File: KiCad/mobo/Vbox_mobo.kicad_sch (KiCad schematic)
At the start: 38 parts, among them J1 Conn_01x02, J2 DuPont Connector, J2 JTAG_TC2030, J4 Conn_01x06, J5 Conn_01x06, J6 Conn_01x10, J7 Conn_01x10, SW1 Boot, U1 XC6206, U2 X05A26H12G, U3 RP2040, U4 W25Q128JVS, Y1 12MHz

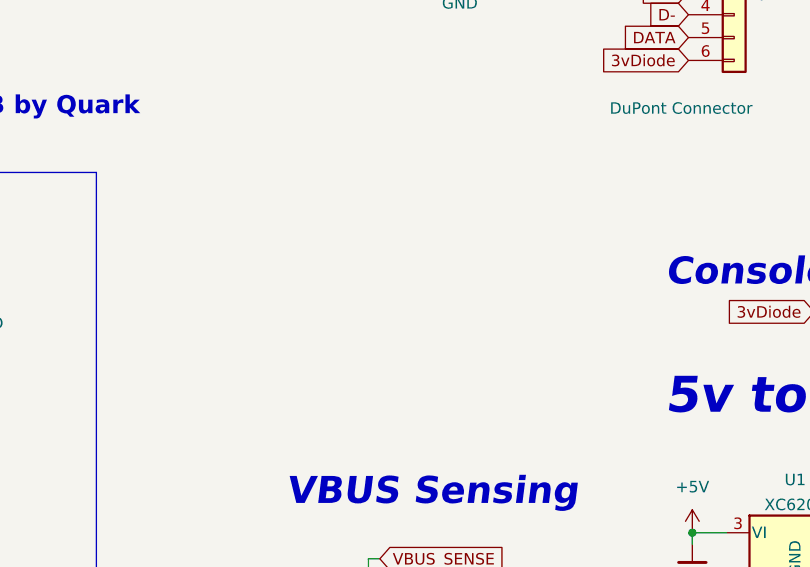
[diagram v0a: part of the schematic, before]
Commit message: replace vias with mounting holes
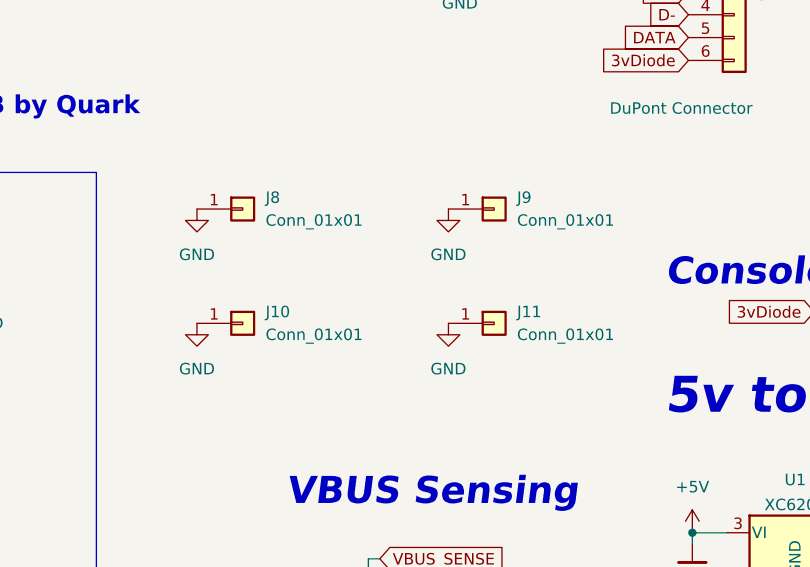
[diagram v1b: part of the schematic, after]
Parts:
- added J10, J11, J8, J9: Conn_01x01, MountingHole:MountingHole_3.2mm_M3_ISO14580_Pad_TopBottom, symbol Connector_Generic:Conn_01x01
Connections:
- net GND: now also J10.1 (Pin_1), J11.1 (Pin_1), J8.1 (Pin_1), J9.1 (Pin_1)
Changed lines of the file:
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@@
+    )
+  )
+  (symbol (lib_id "Connector_Generic:Conn_01x01") (at 190.5 125.73 0) (unit 1)
+    (in_bom yes) (on_board yes) (dnp no) (fields_autoplaced)
+    (property "Reference" "J10" (at 193.04 124.46 0)
+      (effects (font (size 1.27 1.27)) (justify left))
+    )
+    (property "Value" "Conn_01x01" (at 193.04 127 0)
+      (effects (font (size 1.27 1.27)) (justify left))
+    )
+    (property "Footprint" "MountingHole:MountingHole_3.2mm_M3_ISO14580_Pad_TopBottom" (at 190.5 125.73 0)
+      (effects (font (size 1.27 1.27)) hide)
+    )
+    (property "Datasheet" "~" (at 190.5 125.73 0)
+      (effects (font (size 1.27 1.27)) hide)
+    )
+    (pin "1")
+    (instances
+      (project "Vbox_mobo"
+        (path "/9f19960e-6523-4fd2-955a-272ad4648acf"
+          (reference "J10") (unit 1)
+        )
+      )
     )
   )
@@
     )
   )
+  (symbol (lib_name "GND_8") (lib_id "power:GND") (at 213.36 125.73 0) (unit 1)
+    (in_bom yes) (on_board yes) (dnp no) (fields_autoplaced)
+    (property "Reference" "#PWR032" (at 213.36 132.08 0)
+      (effects (font (size 1.27 1.27)) hide)
+    )
+    (property "Value" "GND" (at 213.36 130.81 0)
+      (effects (font (size 1.27 1.27)))
+    )
+    (property "Footprint" "" (at 213.36 125.73 0)
+      (effects (font (size 1.27 1.27)) hide)
+    )
+    (property "Datasheet" "" (at 213.36 125.73 0)
+      (effects (font (size 1.27 1.27)) hide)
+    )
+    (pin "1")
+    (instances
+      (project "Vbox_mobo"
+        (path "/9f19960e-6523-4fd2-955a-272ad4648acf"
+          (reference "#PWR032") (unit 1)
+        )
+      )
+    )
+  )
   (symbol (lib_id "Device:R_Small") (at 208.4578 157.48 90) (unit 1)
     (in_bom yes) (on_board yes) (dnp no)
@@
     )
   )
+  (symbol (lib_id "Connector_Generic:Conn_01x01") (at 190.5 113.03 0) (unit 1)
+    (in_bom yes) (on_board yes) (dnp no) (fields_autoplaced)
+    (property "Reference" "J8" (at 193.04 111.76 0)
+      (effects (font (size 1.27 1.27)) (justify left))
+    )
+    (property "Value" "Conn_01x01" (at 193.04 114.3 0)
+      (effects (font (size 1.27 1.27)) (justify left))
+    )
+    (property "Footprint" "MountingHole:MountingHole_3.2mm_M3_ISO14580_Pad_TopBottom" (at 190.5 113.03 0)
+      (effects (font (size 1.27 1.27)) hide)
+    )
+    (property "Datasheet" "~" (at 190.5 113.03 0)
+      (effects (font (size 1.27 1.27)) hide)
+    )
+    (pin "1")
+    (instances
+      (project "Vbox_mobo"
+        (path "/9f19960e-6523-4fd2-955a-272ad4648acf"
+          (reference "J8") (unit 1)
+        )
+      )
+    )
+  )
   (symbol (lib_id "power:+5V") (at 240.4618 148.9964 0) (unit 1)
     (in_bom yes) (on_board yes) (dnp no) (fields_autoplaced)
@@
     )
   )
+  (symbol (lib_name "GND_6") (lib_id "power:GND") (at 185.42 113.03 0) (unit 1)
+    (in_bom yes) (on_board yes) (dnp no) (fields_autoplaced)
+    (property "Reference" "#PWR013" (at 185.42 119.38 0)
+      (effects (font (size 1.27 1.27)) hide)
+    )
+    (property "Value" "GND" (at 185.42 118.11 0)
+      (effects (font (size 1.27 1.27)))
+    )
+    (property "Footprint" "" (at 185.42 113.03 0)
+      (effects (font (size 1.27 1.27)) hide)
+    )
+    (property "Datasheet" "" (at 185.42 113.03 0)
+      (effects (font (size 1.27 1.27)) hide)
+    )
+    (pin "1")
+    (instances
+      (project "Vbox_mobo"
+        (path "/9f19960e-6523-4fd2-955a-272ad4648acf"
+          (reference "#PWR013") (unit 1)
+        )
+      )
+    )
+  )
   (symbol (lib_id "Memory_Flash:W25Q128JVS") (at 144.145 137.16 0) (unit 1)
     (in_bom yes) (on_board yes) (dnp no)
@@
     )
   )
+  (symbol (lib_id "Connector_Generic:Conn_01x01") (at 218.44 125.73 0) (unit 1)
+    (in_bom yes) (on_board yes) (dnp no) (fields_autoplaced)
+    (property "Reference" "J11" (at 220.98 124.46 0)
+      (effects (font (size 1.27 1.27)) (justify left))
+    )
+    (property "Value" "Conn_01x01" (at 220.98 127 0)
+      (effects (font (size 1.27 1.27)) (justify left))
+    )
+    (property "Footprint" "MountingHole:MountingHole_3.2mm_M3_ISO14580_Pad_TopBottom" (at 218.44 125.73 0)
+      (effects (font (size 1.27 1.27)) hide)
+    )
+    (property "Datasheet" "~" (at 218.44 125.73 0)
+      (effects (font (size 1.27 1.27)) hide)
+    )
+    (pin "1")
+    (instances
+      (project "Vbox_mobo"
+        (path "/9f19960e-6523-4fd2-955a-272ad4648acf"
+          (reference "J11") (unit 1)
+        )
+      )
+    )
+  )
+  (symbol (lib_name "GND_9") (lib_id "power:GND") (at 185.42 125.73 0) (unit 1)
+    (in_bom yes) (on_board yes) (dnp no) (fields_autoplaced)
+    (property "Reference" "#PWR033" (at 185.42 132.08 0)
+      (effects (font (size 1.27 1.27)) hide)
+    )
+    (property "Value" "GND" (at 185.42 130.81 0)
+      (effects (font (size 1.27 1.27)))
+    )
+    (property "Footprint" "" (at 185.42 125.73 0)
+      (effects (font (size 1.27 1.27)) hide)
+    )
+    (property "Datasheet" "" (at 185.42 125.73 0)
+      (effects (font (size 1.27 1.27)) hide)
+    )
+    (pin "1")
+    (instances
+      (project "Vbox_mobo"
+        (path "/9f19960e-6523-4fd2-955a-272ad4648acf"
+          (reference "#PWR033") (unit 1)
+        )
+      )
+    )
+  )
+  (symbol (lib_id "Connector_Generic:Conn_01x01") (at 218.44 113.03 0) (unit 1)
+    (in_bom yes) (on_board yes) (dnp no) (fields_autoplaced)
+    (property "Reference" "J9" (at 220.98 111.76 0)
+      (effects (font (size 1.27 1.27)) (justify left))
+    )
+    (property "Value" "Conn_01x01" (at 220.98 114.3 0)
+      (effects (font (size 1.27 1.27)) (justify left))
+    )
+    (property "Footprint" "MountingHole:MountingHole_3.2mm_M3_ISO14580_Pad_TopBottom" (at 218.44 113.03 0)
+      (effects (font (size 1.27 1.27)) hide)
+    )
+    (property "Datasheet" "~" (at 218.44 113.03 0)
+      (effects (font (size 1.27 1.27)) hide)
+    )
+    (pin "1")
+    (instances
+      (project "Vbox_mobo"
+        (path "/9f19960e-6523-4fd2-955a-272ad4648acf"
+          (reference "J9") (unit 1)
+        )
+      )
+    )
+  )
   (symbol (lib_id "power:GND") (at 74.676 171.704 0) (unit 1)
     (in_bom yes) (on_board yes) (dnp no) (fields_autoplaced)
@@
         )
       )
+    )
+  )
+  (symbol (lib_name "GND_7") (lib_id "power:GND") (at 213.36 113.03 0) (unit 1)
+    (in_bom yes) (on_board yes) (dnp no) (fields_autoplaced)
+    (property "Reference" "#PWR018" (at 213.36 119.38 0)
+      (effects (font (size 1.27 1.27)) hide)
+    )
+    (property "Value" "GND" (at 213.36 118.11 0)
+      (effects (font (size 1.27 1.27)))
+    )
+    (property "Footprint" "" (at 213.36 113.03 0)
+      (effects (font (size 1.27 1.27)) hide)
+    )
+    (property "Datasheet" "" (at 213.36 113.03 0)
+      (effects (font (size 1.27 1.27)) hide)
+    )
+    (pin "1")
+    (instances
+      (project "Vbox_mobo"
+        (path "/9f19960e-6523-4fd2-955a-272ad4648acf"
+          (reference "#PWR018") (unit 1)
+        )
+      )

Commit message: add lcsc pn for mobo connectors
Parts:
- J4, J5: LCSC (none) -> C471518
- J6, J7: LCSC (none) -> C264997
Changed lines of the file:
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@@
+      (effects (font (size 1.27 1.27)) hide)
+    )
+    (property "LCSC" "C471518" (at 104.14 78.74 0)
       (effects (font (size 1.27 1.27)) hide)
     )
@@
     )
     (property "Datasheet" "~" (at 219.71 80.01 0)
+      (effects (font (size 1.27 1.27)) hide)
+    )
+    (property "LCSC" "C471518" (at 219.71 80.01 0)
       (effects (font (size 1.27 1.27)) hide)
     )
@@
       (effects (font (size 1.27 1.27)) hide)
     )
+    (property "LCSC" "C264997" (at 262.89 31.75 0)
+      (effects (font (size 1.27 1.27)) hide)
+    )
     (pin "1")
     (pin "10")
@@
       (effects (font (size 1.27 1.27)) hide)
     )
-    (property "Field4" "" (at 99.06 30.48 0)
-      (effects (font (size 1.27 1.27)) hide)
-    )
+    (property "LCSC" "C264997" (at 99.06 30.48 0)
+      (effects (font (size 1.27 1.27)) hide)
+    )

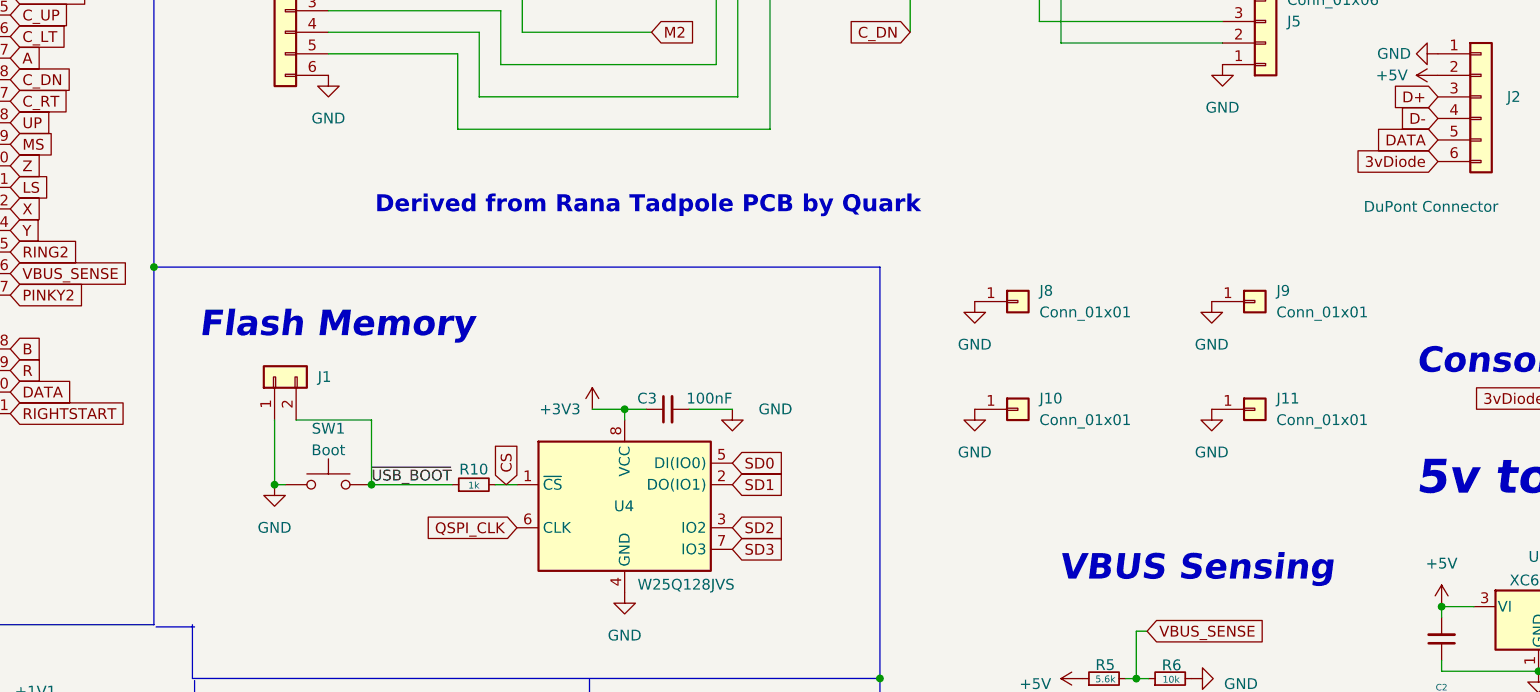
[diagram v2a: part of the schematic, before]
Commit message: add 4 3.3v power headers
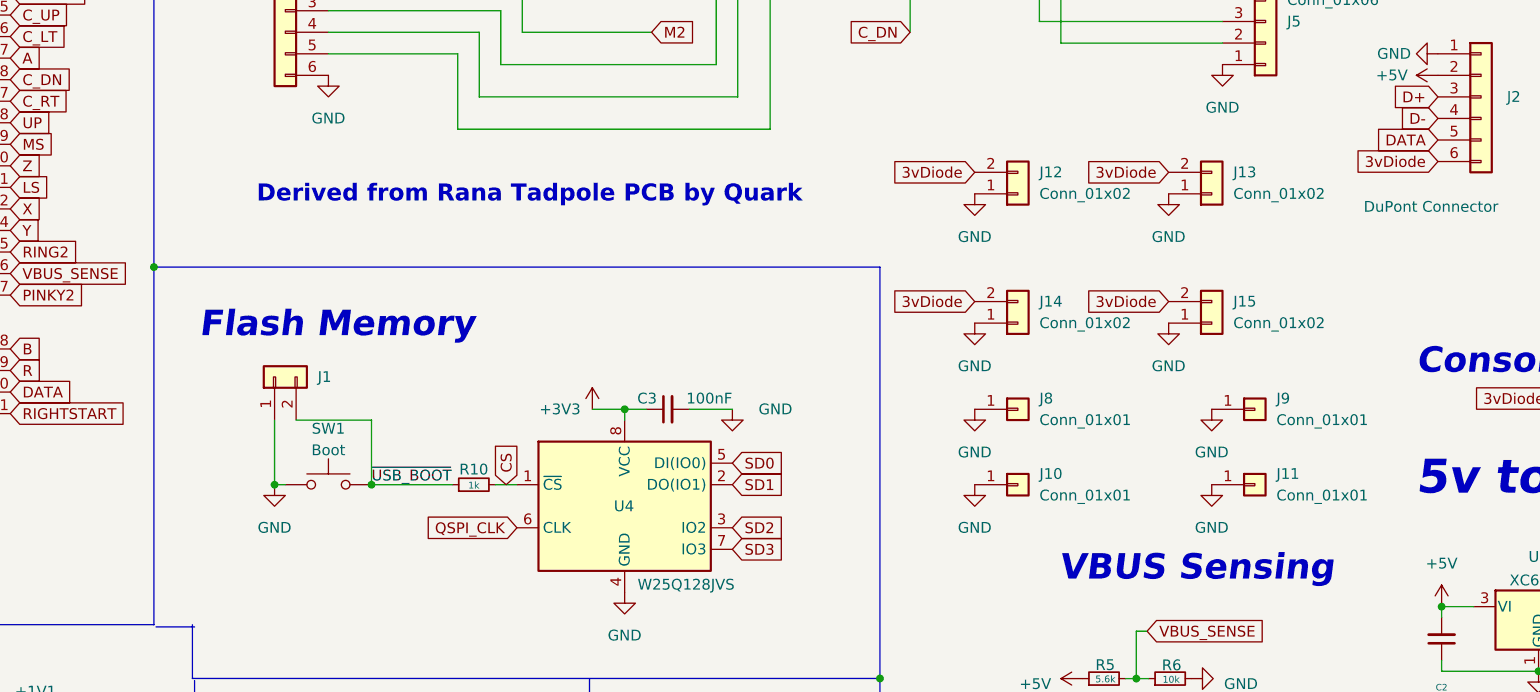
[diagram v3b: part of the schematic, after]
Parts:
- added J12, J13, J14, J15: Conn_01x02, Connector_PinHeader_2.00mm:PinHeader_1x02_P2.00mm_Vertical, symbol Connector_Generic:Conn_01x02
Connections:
- net +3V3: now also J12.2 (Pin_2), J13.2 (Pin_2), J14.2 (Pin_2), J15.2 (Pin_2)
- net GND: now also J12.1 (Pin_1), J13.1 (Pin_1), J14.1 (Pin_1), J15.1 (Pin_1)
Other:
- moved on the sheet: J10, J11, J8, J9

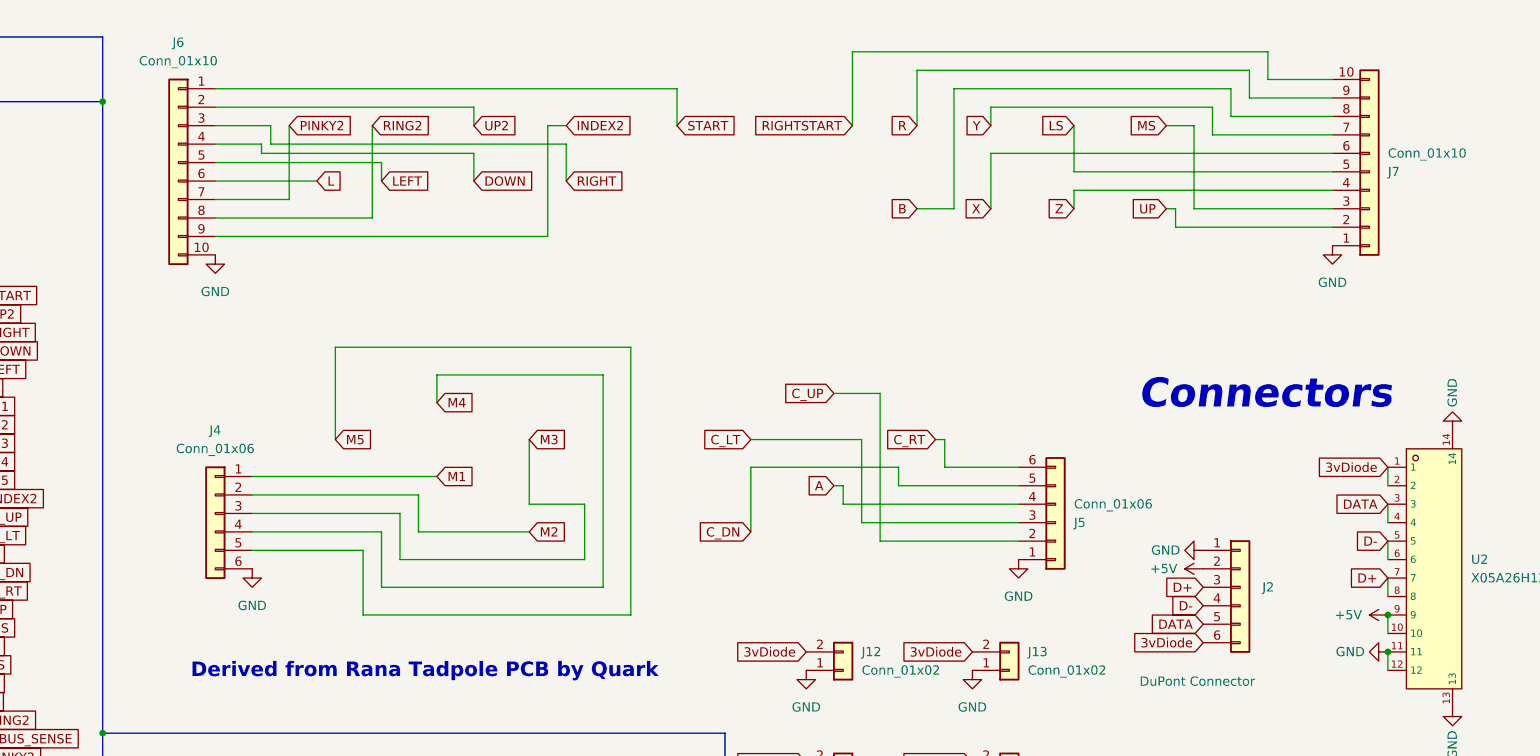
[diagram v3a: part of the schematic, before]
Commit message: flip connectors
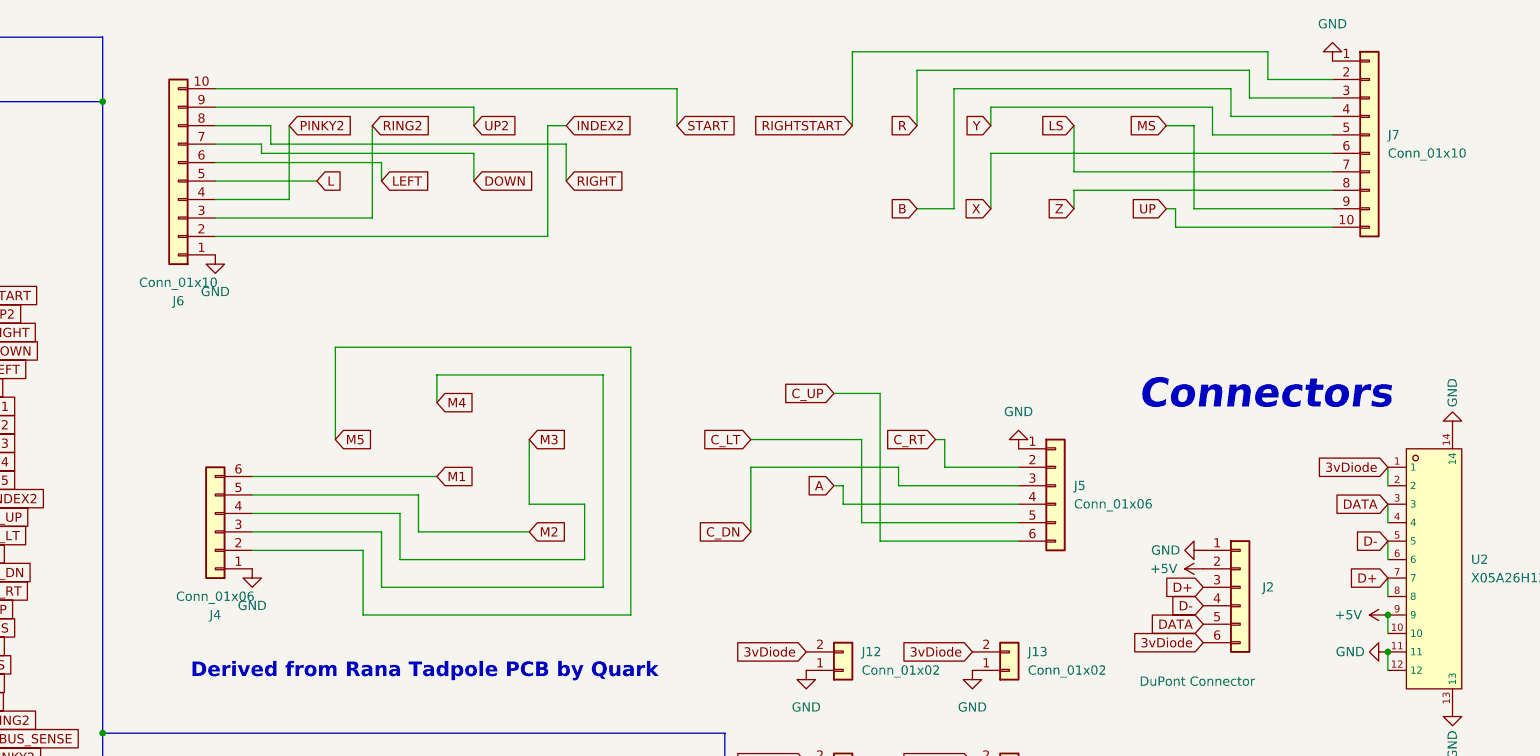
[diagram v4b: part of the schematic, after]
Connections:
- net B: now also J7.4 (Pin_4); no longer J7.8 (Pin_8)
- net C_DN: now also J5.3 (Pin_3); no longer J5.5 (Pin_5)
- net C_LT: now also J5.5 (Pin_5); no longer J5.3 (Pin_3)
- net C_RT: now also J5.2 (Pin_2); no longer J5.6 (Pin_6)
- net C_UP: now also J5.6 (Pin_6); no longer J5.2 (Pin_2)
- net DOWN: now also J6.7 (Pin_7); no longer J6.4 (Pin_4)
- net GND: now also J4.1 (Pin_1), J6.1 (Pin_1); no longer J4.6 (Pin_6), J6.10 (Pin_10)
- net INDEX2: now also J6.2 (Pin_2); no longer J6.9 (Pin_9)
- net L: now also J6.5 (Pin_5); no longer J6.6 (Pin_6)
- net LEFT: now also J6.6 (Pin_6); no longer J6.5 (Pin_5)
- net LS: now also J7.7 (Pin_7); no longer J7.5 (Pin_5)
- net M1: now also J4.6 (Pin_6); no longer J4.1 (Pin_1)
- net M2: now also J4.5 (Pin_5); no longer J4.2 (Pin_2)
- net M3: now also J4.4 (Pin_4); no longer J4.3 (Pin_3)
- net M4: now also J4.3 (Pin_3); no longer J4.4 (Pin_4)
- net M5: now also J4.2 (Pin_2); no longer J4.5 (Pin_5)
- net MS: now also J7.9 (Pin_9); no longer J7.3 (Pin_3)
- net PINKY2: now also J6.4 (Pin_4); no longer J6.7 (Pin_7)
- net R: now also J7.3 (Pin_3); no longer J7.9 (Pin_9)
- net RIGHT: now also J6.8 (Pin_8); no longer J6.3 (Pin_3)
- net RIGHTSTART: now also J7.2 (Pin_2); no longer J7.10 (Pin_10)
- net RING2: now also J6.3 (Pin_3); no longer J6.8 (Pin_8)
- net START: now also J6.10 (Pin_10); no longer J6.1 (Pin_1)
- net UP: now also J7.10 (Pin_10); no longer J7.2 (Pin_2)
- net UP2: now also J6.9 (Pin_9); no longer J6.2 (Pin_2)
- net Y: now also J7.5 (Pin_5); no longer J7.7 (Pin_7)
- net Z: now also J7.8 (Pin_8); no longer J7.4 (Pin_4)
